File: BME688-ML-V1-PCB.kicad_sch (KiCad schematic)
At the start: 29 parts, among them SW1 434133025816, U1 STM32L431KBU6TR, U2 BME688

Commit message: remove dependency on global library
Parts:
- C1, C2, C3, C4, C5, C6, C7: footprint 1GlobalFootprintsLibrary:C_0603_nominal -> 1projectLibrary:C_0603_nominal
- CONN3: symbol 1GlobalSymbolsLibrary:microSdCard -> 1projectLibrary:microSdCard
- R1, R2, R3, R4, R5, R6, R7, R8: footprint 1GlobalFootprintsLibrary:R_0603_nominal -> 1projectLibrary:R_0603_nominal
- U2: symbol 1projectLibrary:BME680 -> 1projectLibrary:BME688; MANUFACTURER (none) -> Bosch Sensortec; MPN (none) -> BME680; manufacturer (none) -> Bosch Sensortec; supplier1Name (none) -> Mouser; supplier1PartNumber (none) -> 262-BME680; supplier1PartURL (none) -> https://www.mouser.be/ProductDetail/Bosch-Sensortec/BME680?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; supplier2Name (none) -> Digi-Key; supplier2PartNumber (none) -> 828-1077-1-ND; supplier2PartURL (none) -> https://www.digikey.be/nl/products/detail/bosch-sensortec/B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
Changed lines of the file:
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@@
 	)
 	(symbol
-		(lib_id "1GlobalSymbolsLibrary:microSdCard")
+		(lib_id "1projectLibrary:microSdCard")
 		(at 231.14 96.52 0)
 		(unit 1)
@@
 		)
 		(property "Datasheet" "https://www.mouser.be/datasheet/2/670/msd_1_a-3367597.pdf"
-			(at 226.06 92.71 0)
+			(at 231.14 119.38 0)
 			(effects
 				(font
@@
 		)
 		(property "Description" "micro-SD card slot"
-			(at 231.14 109.474 0)
+			(at 231.14 109.22 0)
 			(effects
 				(font
@@
 		)
 		(property "manufacturerName" "CUI Devices"
-			(at 231.14 83.82 0)
+			(at 231.14 111.76 0)
 			(effects
 				(font
@@
 		)
 		(property "mouserPartNumber" "179-MSD-1-A"
-			(at 230.886 109.474 0)
+			(at 231.14 114.3 0)
 			(effects
 				(font
@@
 		)
 		(property "manufacturerPartNumber" "MSD-1-A"
-			(at 234.188 106.934 0)
+			(at 231.14 116.84 0)
 			(effects
 				(font
 					(size 1.27 1.27)
 				)
+				(hide yes)
 			)
 		)
@@
 			)
 		)
-		(property "Footprint" "1GlobalFootprintsLibrary:C_0603_nominal"
+		(property "Footprint" "1projectLibrary:C_0603_nominal"
 			(at 72.0852 59.69 0)
 			(effects
@@
 			)
 		)
-		(property "Footprint" "1GlobalFootprintsLibrary:R_0603_nominal"
+		(property "Footprint" "1projectLibrary:R_0603_nominal"
 			(at 35.052 148.59 90)
 			(effects
@@
 			)
 		)
-		(property "Footprint" "1GlobalFootprintsLibrary:C_0603_nominal"
+		(property "Footprint" "1projectLibrary:C_0603_nominal"
 			(at 82.2452 59.69 0)
 			(effects
@@
 	)
 	(symbol
-		(lib_id "1projectLibrary:BME680")
+		(lib_id "1projectLibrary:BME688")
 		(at 231.14 55.88 0)
 		(unit 1)
@@
 			)
 		)
-		(property "Datasheet" "https://www.bosch-sensortec.com/media/boschsensortec/downloads/datasheets/bst-bme688-ds000.pdf"
+		(property "Datasheet" "https://ae-bst.resource.bosch.com/media/_tech/media/datasheets/BST-BME680-DS001.pdf"
 			(at 226.06 27.94 0)
 			(effects
@@
 			)
 		)
+		(property "manufacturer" "Bosch Sensortec"
+			(at 231.14 12.7 0)
+			(effects
+				(font
+					(size 1.27 1.27)
+				)
+				(hide yes)
+			)
+		)
+		(property "supplier1Name" "Mouser"
+			(at 231.14 17.78 0)
+			(effects
+				(font
+					(size 1.27 1.27)
+				)
+				(hide yes)
+			)
+		)
+		(property "supplier1PartNumber" "262-BME680"
+			(at 231.14 15.24 0)
+			(effects
+				(font
+					(size 1.27 1.27)
+				)
+				(hide yes)
+			)
+		)
+		(property "supplier1PartURL" "https://www.mouser.be/ProductDetail/Bosch-Sensortec/BME680?qs=v271MhAjFHjo0yA%2FC4OnDQ%3D%3D"
+			(at 229.87 26.67 0)
+			(effects
+				(font
+					(size 1.27 1.27)
+				)
+				(hide yes)
+			)
+		)
+		(property "supplier2Name" "Digi-Key"
+			(at 229.87 19.05 0)
+			(effects
+				(font
+					(size 1.27 1.27)
+				)
+				(hide yes)
+			)
+		)
+		(property "supplier2PartNumber" "828-1077-1-ND"
+			(at 229.87 7.62 0)
+			(effects
+				(font
+					(size 1.27 1.27)
+				)
+				(hide yes)
+			)
+		)
+		(property "supplier2PartURL" "https://www.digikey.be/nl/products/detail/bosch-sensortec/BME680/7401317"
+			(at 232.41 24.13 0)
+			(effects
+				(font
+					(size 1.27 1.27)
+				)
+				(hide yes)
+			)
+		)
+		(property "MPN" "BME680"
+			(at 231.14 10.16 0)
+			(effects
+				(font
+					(size 1.27 1.27)
+				)
+				(hide yes)
+			)
+		)
+		(property "remark" ""
+			(at 231.14 55.88 0)
+			(effects
+				(font
+					(size 1.27 1.27)
+				)
+				(hide yes)
+			)
+		)
+		(property "MANUFACTURER" "Bosch Sensortec"
+			(at 231.14 7.62 0)
+			(effects
+				(font
+					(size 1.27 1.27)
+				)
+				(hide yes)
+			)
+		)
+		(property "OctoPartURL" ""
+			(at 231.14 55.88 0)
+			(effects
+				(font
+					(size 1.27 1.27)
+				)
+				(hide yes)
+			)
+		)
 		(pin "1"
 		)
@@
 			)
 		)
-		(property "Footprint" "1GlobalFootprintsLibrary:C_0603_nominal"
+		(property "Footprint" "1projectLibrary:C_0603_nominal"
 			(at 92.4052 59.69 0)
 			(effects
@@
 			)
 		)
-		(property "Footprint" "1GlobalFootprintsLibrary:R_0603_nominal"
+		(property "Footprint" "1projectLibrary:R_0603_nominal"
 			(at 231.902 30.48 90)
 			(effects
@@
 			)
 		)
-		(property "Footprint" "1GlobalFootprintsLibrary:R_0603_nominal"
+		(property "Footprint" "1projectLibrary:R_0603_nominal"
 			(at 212.852 81.28 90)
 			(effects
@@
 			)
 		)
-		(property "Footprint" "1GlobalFootprintsLibrary:R_0603_nominal"
+		(property "Footprint" "1projectLibrary:R_0603_nominal"
 			(at 205.232 81.28 90)
 			(effects
@@
 			)
 		)
-		(property "Footprint" "1GlobalFootprintsLibrary:R_0603_nominal"
+		(property "Footprint" "1projectLibrary:R_0603_nominal"
 			(at 209.042 81.28 90)
 			(effects
@@
 			)
 		)
-		(property "Footprint" "1GlobalFootprintsLibrary:C_0603_nominal"
+		(property "Footprint" "1projectLibrary:C_0603_nominal"
 			(at 88.5952 78.74 0)
 			(effects
@@
 			)
 		)
-		(property "Footprint" "1GlobalFootprintsLibrary:C_0603_nominal"
+		(property "Footprint" "1projectLibrary:C_0603_nominal"
 			(at 254.9652 96.52 0)
 			(effects
@@
 			)
 		)
-		(property "Footprint" "1GlobalFootprintsLibrary:C_0603_nominal"
+		(property "Footprint" "1projectLibrary:C_0603_nominal"
 			(at 249.8852 60.96 0)
 			(effects
@@
 			)
 		)
-		(property "Footprint" "1GlobalFootprintsLibrary:R_0603_nominal"
+		(property "Footprint" "1projectLibrary:R_0603_nominal"
 			(at 201.422 81.28 90)
 			(effects
@@
 			)
 		)
-		(property "Footprint" "1GlobalFootprintsLibrary:R_0603_nominal"
+		(property "Footprint" "1projectLibrary:R_0603_nominal"
 			(at 37.592 148.59 90)
 			(effects
@@
 			)
 		)
-		(property "Footprint" "1GlobalFootprintsLibrary:C_0603_nominal"
+		(property "Footprint" "1projectLibrary:C_0603_nominal"
 			(at 246.0752 96.52 0)
 			(effects
@@
 			)
 		)
-		(property "Footprint" "1GlobalFootprintsLibrary:R_0603_nominal"
+		(property "Footprint" "1projectLibrary:R_0603_nominal"
 			(at 216.662 81.28 90)
 			(effects

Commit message: remove dependencies on global library
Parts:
- SW1: footprint 1GlobalFootprintsLibrary:Wurth-434133025816 -> 1projectLibrary:Wurth-434133025816; symbol 1GlobalSymbolsLibrary:Switch_434133025816 -> 1projectLibrary:Switch_434133025816
- U2: footprint 1GlobalFootprintsLibrary:BME680 -> 1projectLibrary:BME688
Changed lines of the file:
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@@
 			)
 		)
-		(property "Footprint" "1GlobalFootprintsLibrary:BME680"
+		(property "Footprint" "1projectLibrary:BME688"
 			(at 267.97 67.31 0)
 			(effects
@@
 	)
 	(symbol
-		(lib_id "1GlobalSymbolsLibrary:Switch_434133025816")
+		(lib_id "1projectLibrary:Switch_434133025816")
 		(at 74.93 74.93 0)
 		(unit 1)
@@
 			)
 		)
-		(property "Footprint" "1GlobalFootprintsLibrary:Wurth-434133025816"
+		(property "Footprint" "1projectLibrary:Wurth-434133025816"
 			(at 75.692 91.694 0)
 			(effects

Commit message: fix
Tie BOOT0/PH3 to GND, as without the SW is not running stable..
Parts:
- U1: footprint 1projectLibrary:STM32-QFN-32-1EP -> Package_DFN_QFN:QFN-32-1EP_5x5mm_P0.5mm_EP3.45x3.45mm
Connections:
- net GND: now also U1.31 (BOOT0)
- no-connect marks 14 -> 13
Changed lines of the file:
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@@
+	)
+	(junction
+		(at 87.63 80.01)
+		(diameter 0)
+		(color 0 0 0 0)
 	)
 	(junction
@@
 	)
 	(no_connect
-		(at 97.79 73.66)
-	)
-	(no_connect
 		(at 133.35 96.52)
 	)
@@
 	(wire
 		(pts
+			(xy 97.79 73.66) (xy 95.25 73.66)
+		)
+		(stroke
+			(width 0)
+			(type default)
+		)
+	)
+	(wire
+		(pts
 			(xy 52.07 139.7) (xy 87.63 139.7)
 		)
@@
 	(wire
 		(pts
+			(xy 95.25 73.66) (xy 95.25 80.01)
+		)
+		(stroke
+			(width 0)
+			(type default)
+		)
+	)
+	(wire
+		(pts
 			(xy 231.14 45.72) (xy 231.14 36.83)
 		)
@@
 		(pts
 			(xy 210.82 85.09) (xy 210.82 96.52)
+		)
+		(stroke
+			(width 0)
+			(type default)
+		)
+	)
+	(wire
+		(pts
+			(xy 95.25 80.01) (xy 87.63 80.01)
 		)
 		(stroke
@@
 			)
 		)
-		(property "Footprint" "1projectLibrary:STM32-QFN-32-1EP"
+		(property "Footprint" "Package_DFN_QFN:QFN-32-1EP_5x5mm_P0.5mm_EP3.45x3.45mm"
 			(at 149.86 124.46 0)
 			(effects

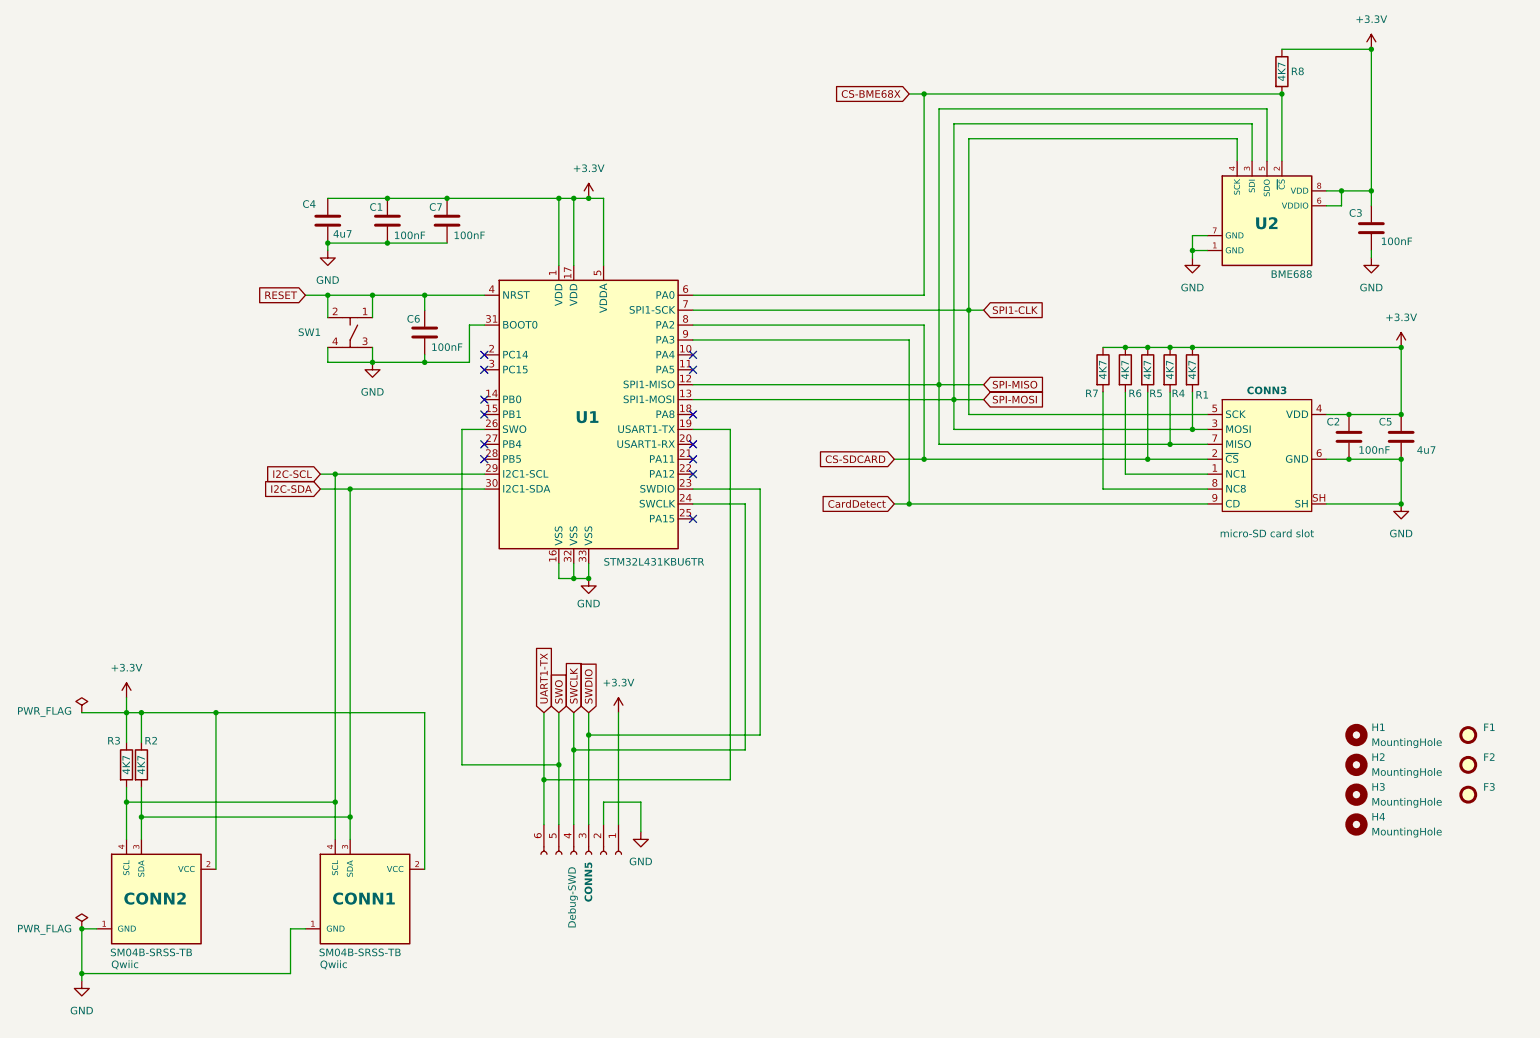
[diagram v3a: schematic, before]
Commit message: Redesign for V1.2
Moved BME688 onto its own I2C bus.
Placed 2 BME688
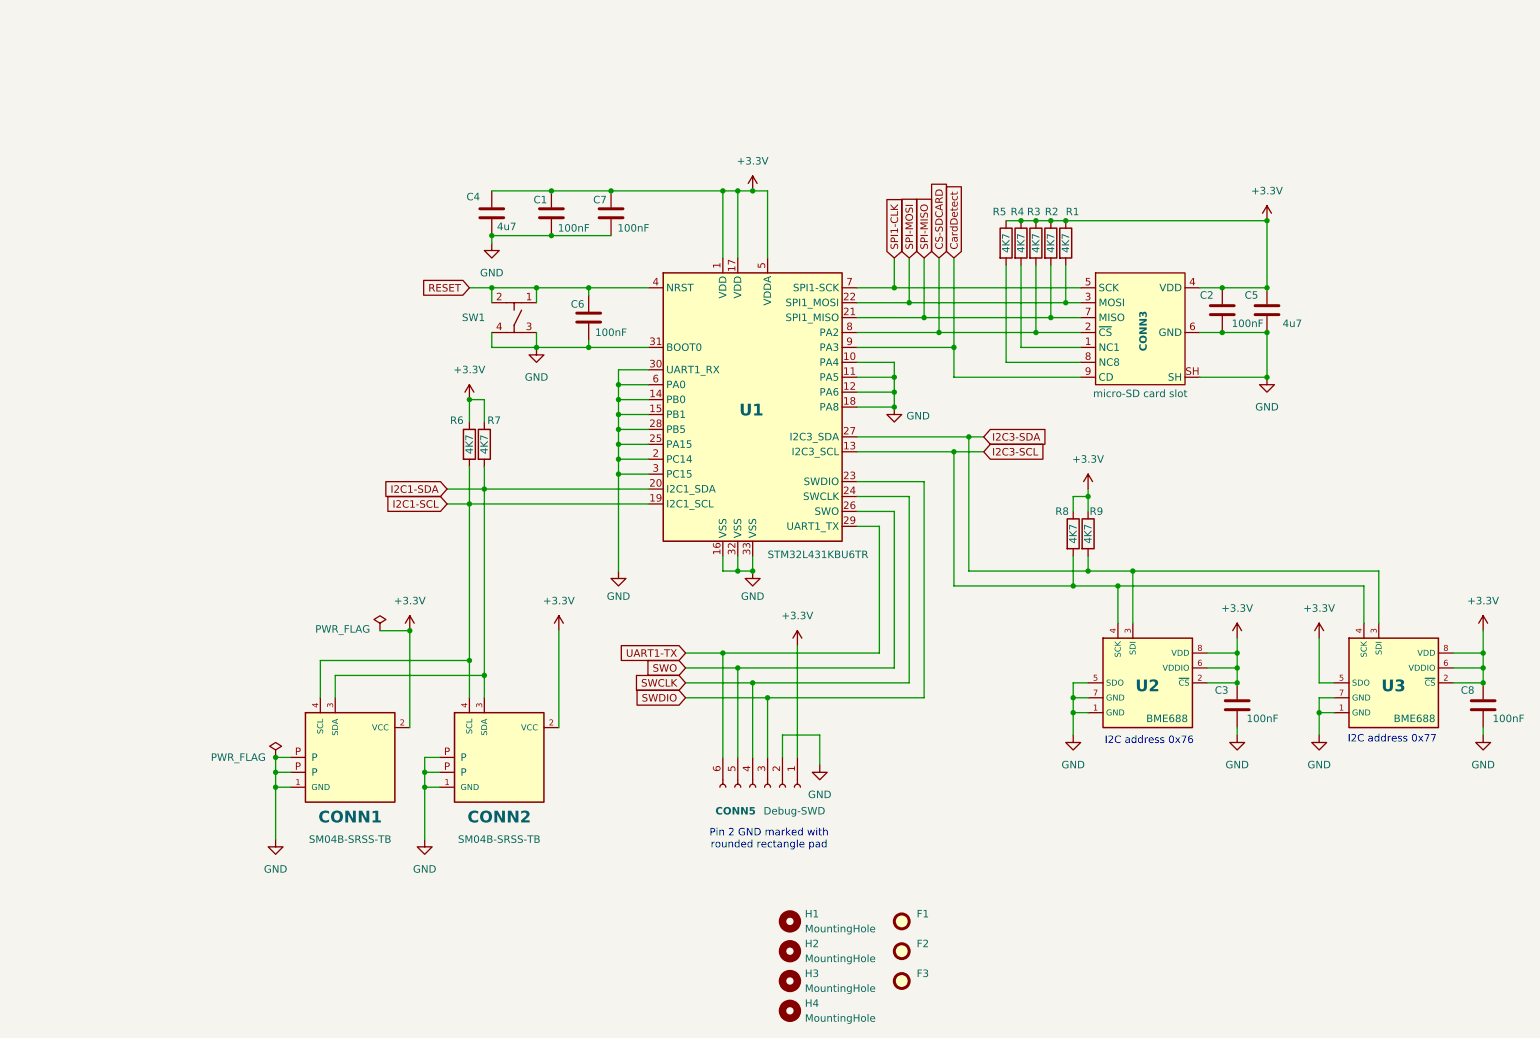
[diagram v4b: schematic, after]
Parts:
- removed CONN1, CONN2: SM04B-SRSS-TB, 1projectLibrary:JST_SH_SM04B-SRSS-TB_1x04-1MP_P1.00mm_Horizontal, symbol 1projectLibrary:Qwiic
- added C8: KGM15AR71C104KT, 1projectLibrary:C_0603_nominal, symbol Device:C
- added CONN1, CONN2: SM04B-SRSS-TB, 1projectLibrary:JST_SH_SM04B-SRSS-TB_1x04-1MP_P1.00mm_Horizontal, symbol 1projectLibrary:Qwiic connector
- added R9: CR0603-FX-4701ELF, 1projectLibrary:R_0603_nominal, symbol Device:R
- added U3: BME688, 1projectLibrary:BME688, symbol 1projectLibrary:BME688
- CONN3: footprint 1GlobalFootprintsLibrary:MSD-1-A -> 1projectLibrary:MSD-1-A
- F1, F2, F3: footprint Fiducial:Fiducial_0.75mm_Mask1.5mm -> Fiducial:Fiducial_0.5mm_Mask1mm
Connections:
- net +3.3V: now also U2.2 (~{CS}), C8.1, CONN1.2 (VCC), CONN2.2 (VCC), R9.1, U3.2 (~{CS}), U3.5 (SDO), U3.6 (VDDIO), U3.8 (VDD)
- net CS-SDCARD: now also R3.2; no longer R5.2
- net GND: now also U1.10 (PA4), U1.11 (PA5), U1.12 (PA6), U1.14 (PB0), U1.15 (PB1), U1.18 (PA8), U1.2 (PC14), U1.25 (PA15), U1.28 (PB5), U1.3 (PC15), U1.30 (UART1_RX), U1.6 (PA0), U2.5 (SDO), C8.2, CONN1.1 (GND), CONN1.P, CONN2.1 (GND), CONN2.P, U3.1 (GND), U3.7 (GND)
- net SPI-MISO: now also R2.2, U1.21 (SPI1_MISO); no longer R4.2, U1.12 (SPI1-MISO), U2.5 (SDO)
- net SPI-MOSI: now also U1.22 (SPI1_MOSI); no longer U1.13 (SPI1-MOSI), U2.3 (SDI)
- net SPI1-CLK: no longer U2.4 (SCK)
- net UART1-TX: now also U1.29 (UART1_TX); no longer U1.19 (USART1-TX)
- net at CONN3.1 (NC1): now also R4.2; no longer R6.2
- net at CONN3.8 (NC8): now also R5.2; no longer R7.2
- net I2C1-SDA: now reaches U1.20 (I2C1_SDA)
- net I2C1-SDA: now also R7.2, CONN1.3 (SDA), CONN2.3 (SDA)
- net I2C3-SDA: now reaches U1.27 (I2C3_SDA)
- net I2C3-SDA: now also U2.3 (SDI), R9.2, U3.3 (SDI)
- removed net CS-BME68X: R8.2, U1.6 (PA0), U2.2 (~{CS})
- removed net I2C-SCL: R3.2, U1.29 (I2C1-SCL)
- removed net I2C-SDA: R2.2, U1.30 (I2C1-SDA)
- new net I2C1-SCL: CONN1.4 (SCL), CONN2.4 (SCL), R6.2, U1.19 (I2C1_SCL)
- new net I2C3-SCL: R8.2, U1.13 (I2C3_SCL), U2.4 (SCK), U3.4 (SCK)
- no-connect marks 13 -> 0
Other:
- note added: "I2C address 0x76"
- note added: "I2C address 0x77"
- note added: "Pin 2 GND marked with rounded rectangle pad"
- moved on the sheet: C1, C2, C3, C4, C5, C6, C7, CONN3, CONN5, F1, F2, F3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

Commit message: updating BOM
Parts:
- C1, C2, C3, C6, C7, C8: MPN (none) -> KGM15AR71C104KT
- C4, C5: MPN (none) -> C0603C475K8PAC7411
- CONN1, CONN2: MPN (none) -> SM04B-SRSS-TB
- CONN3: MPN (none) -> MSD-1-A
- R1, R2, R3, R4, R5, R6, R7, R8, R9: MPN (none) -> CR0603-FX-4701ELF
- SW1: MPN (none) -> 434133025816
- U1: MPN (none) -> STM32L431KBU6TR
- U2, U3: MPN BME680 -> BME688
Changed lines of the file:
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@@
 			)
 		)
+		(property "MPN" "SM04B-SRSS-TB"
+			(at 74.93 147.32 0)
+			(effects
+				(font
+					(size 1.27 1.27)
+				)
+				(hide yes)
+			)
+		)
 		(pin "2"
 		)
@@
 			)
 		)
+		(property "MPN" "MSD-1-A"
+			(at 209.55 74.93 0)
+			(effects
+				(font
+					(size 1.27 1.27)
+				)
+				(hide yes)
+			)
+		)
 		(pin "2"
 		)
@@
 			)
 		)
+		(property "MPN" "C0603C475K8PAC7411"
+			(at 99.06 54.61 0)
+			(effects
+				(font
+					(size 1.27 1.27)
+				)
+				(hide yes)
+			)
+		)
 		(pin "2"
 		)
@@
 			)
 		)
+		(property "MPN" "STM32L431KBU6TR"
+			(at 143.51 87.63 0)
+			(effects
+				(font
+					(size 1.27 1.27)
+				)
+				(hide yes)
+			)
+		)
 		(pin "9"
 		)
@@
 			)
 		)
+		(property "MPN" "CR0603-FX-4701ELF"
+			(at 191.77 59.69 0)
+			(effects
+				(font
+					(size 1.27 1.27)
+				)
+				(hide yes)
+			)
+		)
 		(pin "1"
 		)
@@
 			)
 		)
+		(property "MPN" "KGM15AR71C104KT"
+			(at 109.22 54.61 0)
+			(effects
+				(font
+					(size 1.27 1.27)
+				)
+				(hide yes)
+			)
+		)
 		(pin "2"
 		)
@@
 			)
 		)
-		(property "MPN" "BME680"
+		(property "MPN" "BME688"
 			(at 210.82 88.9 0)
 			(effects
@@
 			)
 		)
+		(property "MPN" "KGM15AR71C104KT"
+			(at 119.38 54.61 0)
+			(effects
+				(font
+					(size 1.27 1.27)
+				)
+				(hide yes)
+			)
+		)
 		(pin "2"
 		)
@@
 			)
 		)
+		(property "MPN" "KGM15AR71C104KT"
+			(at 267.97 138.43 0)
+			(effects
+				(font
+					(size 1.27 1.27)
+				)
+				(hide yes)
+			)
+		)
 		(pin "2"
 		)
@@
 			)
 		)
+		(property "MPN" "CR0603-FX-4701ELF"
+			(at 189.23 59.69 0)
+			(effects
+				(font
+					(size 1.27 1.27)
+				)
+				(hide yes)
+			)
+		)
 		(pin "1"
 		)
@@
 			)
 		)
+		(property "MPN" "CR0603-FX-4701ELF"
+			(at 95.25 93.98 0)
+			(effects
+				(font
+					(size 1.27 1.27)
+				)
+				(hide yes)
+			)
+		)
 		(pin "1"
 		)
@@
 			)
 		)
+		(property "MPN" "CR0603-FX-4701ELF"
+			(at 186.69 59.69 0)
+			(effects
+				(font
+					(size 1.27 1.27)
+				)
+				(hide yes)
+			)
+		)
 		(pin "1"
 		)
@@
 			)
 		)
-		(property "MPN" "BME680"
+		(property "MPN" "BME688"
 			(at 252.73 88.9 0)
 			(effects
@@
 			)
 		)
+		(property "MPN" "KGM15AR71C104KT"
+			(at 115.57 72.39 0)
+			(effects
+				(font
+					(size 1.27 1.27)
+				)
+				(hide yes)
+			)
+		)
 		(pin "2"
 		)
@@
 			)
 		)
+		(property "MPN" "C0603C475K8PAC7411"
+			(at 231.14 71.12 0)
+			(effects
+				(font
+					(size 1.27 1.27)
+				)
+				(hide yes)
+			)
+		)
 		(pin "2"
 		)
@@
 			)
 		)
+		(property "MPN" "SM04B-SRSS-TB"
+			(at 100.33 147.32 0)
+			(effects
+				(font
+					(size 1.27 1.27)
+				)
+				(hide yes)
+			)
+		)
 		(pin "2"
 		)
@@
 			)
 		)
+		(property "MPN" "KGM15AR71C104KT"
+			(at 226.06 138.43 0)
+			(effects
+				(font
+					(size 1.27 1.27)
+				)
+				(hide yes)
+			)
+		)
 		(pin "2"
 		)
@@
 			)
 		)
+		(property "MPN" "CR0603-FX-4701ELF"
+			(at 97.79 93.98 0)
+			(effects
+				(font
+					(size 1.27 1.27)
+				)
+				(hide yes)
+			)
+		)
 		(pin "1"
 		)
@@
 			)
 		)
+		(property "MPN" "CR0603-FX-4701ELF"
+			(at 194.31 59.69 0)
+			(effects
+				(font
+					(size 1.27 1.27)
+				)
+				(hide yes)
+			)
+		)
 		(pin "1"
 		)
@@
 			)
 		)
+		(property "MPN" "CR0603-FX-4701ELF"
+			(at 198.12 109.22 0)
+			(effects
+				(font
+					(size 1.27 1.27)
+				)
+				(hide yes)
+			)
+		)
 		(pin "1"
 		)
@@
 			)
 		)
+		(property "MPN" "434133025816"
+			(at 102.87 72.39 0)
+			(effects
+				(font
+					(size 1.27 1.27)
+				)
+				(hide yes)
+			)
+		)
 		(pin "1"
 		)
@@
 			)
 		)
+		(property "MPN" "CR0603-FX-4701ELF"
+			(at 200.66 109.22 0)
+			(effects
+				(font
+					(size 1.27 1.27)
+				)
+				(hide yes)
+			)
+		)
 		(pin "1"
 		)
@@
 			)
 		)
+		(property "MPN" "KGM15AR71C104KT"
+			(at 223.52 71.12 0)
+			(effects
+				(font
+					(size 1.27 1.27)
+				)
+				(hide yes)
+			)
+		)
 		(pin "2"
 		)
@@
 			(at 196.85 59.69 0)
 			(effects
+				(font
+					(size 1.27 1.27)
+				)
+				(hide yes)
+			)
+		)
+		(property "MPN" "CR0603-FX-4701ELF"
+			(at 196.85 59.69 0)
+			(effects
